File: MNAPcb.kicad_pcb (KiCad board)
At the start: 2 copper layers, 113.4 x 103.3 mm, 138 parts, among them J1 Conn_01x03_Pin, J2 DA15_Socket, J3 USB_C_Receptacle_USB2.0_16P, J5 Conn_01x02, J7 Conn_01x02, J8 Conn_01x04_Pin, J9 Conn_01x02, SW1 SW_Push_Shielded, U1 STM32F407VGTx, U10 USBLC6-2SC6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

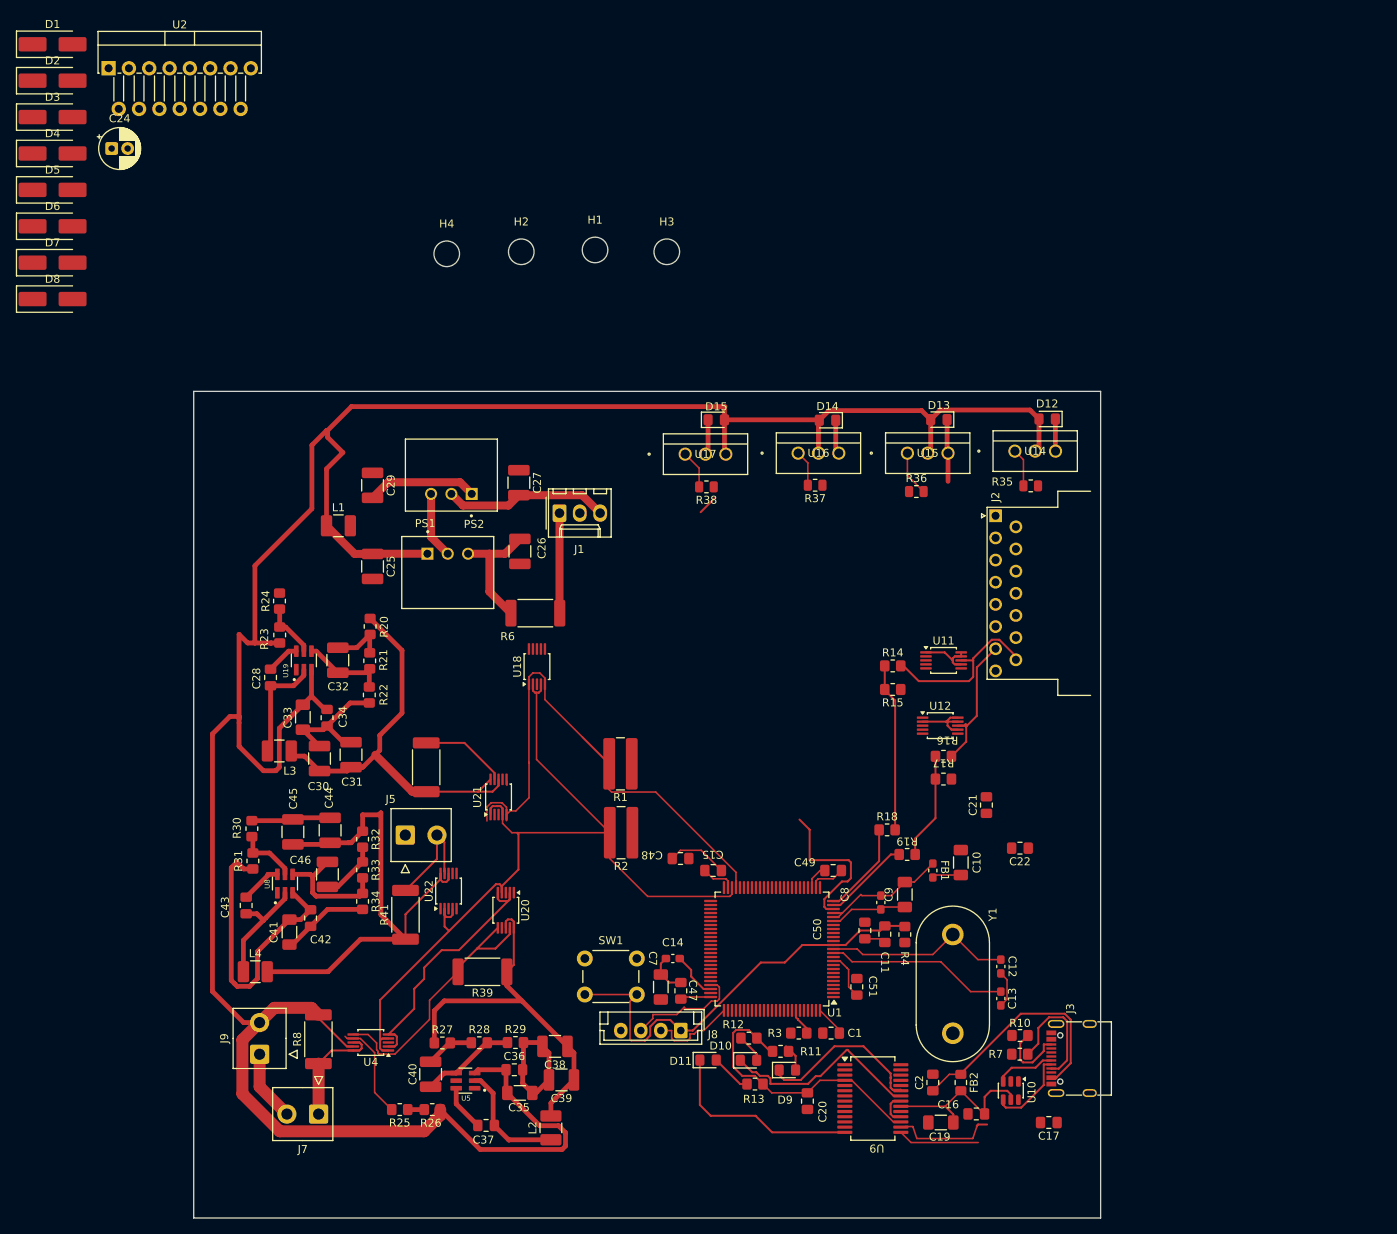
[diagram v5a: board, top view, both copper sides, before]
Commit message: Used Zones and Net
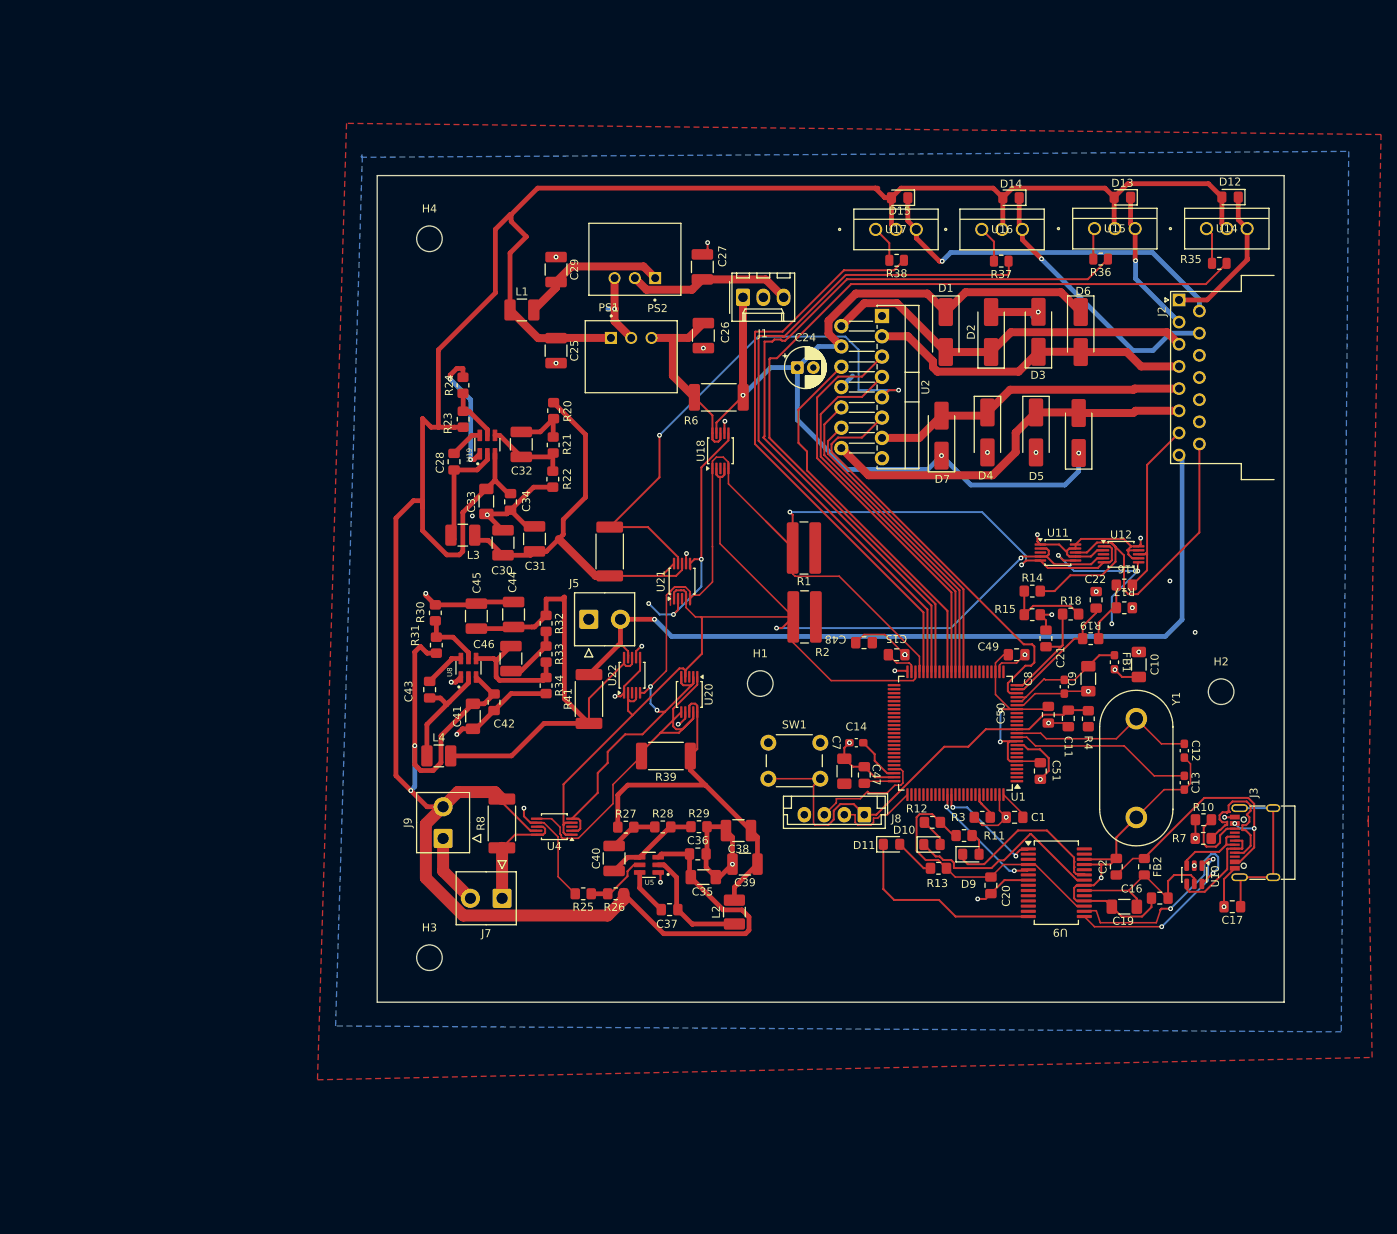
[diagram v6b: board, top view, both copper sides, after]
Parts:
- moved D8 129.4 mm to (170.1, 68.6), turned to 90 degrees
- moved D6 129.2 mm to (170.4, 56.0), turned to -90 degrees
- moved D5 126.6 mm to (164.8, 68.6), turned to -90 degrees
- moved D3 126.1 mm to (165.1, 56.0), turned to 90 degrees
- moved D4 122.0 mm to (158.7, 68.6), turned to -90 degrees
- moved D2 121.5 mm to (159.2, 56.0), turned to 90 degrees
- moved D1 117.3 mm to (153.5, 56.0), turned to -90 degrees
- moved D7 113.2 mm to (153.0, 69.0), turned to 90 degrees
- moved H2 103.3 mm to (187.9, 101.0)
- moved U2 101.5 mm to (145.5, 54.0), turned to -90 degrees
- moved H3 93.1 mm to (89.0, 134.2)
- moved C24 90.0 mm to (134.9, 60.5)
- moved H1 58.0 mm to (130.3, 99.9)
- moved R36 37.1 mm to (172.8, 46.9), turned to 180 degrees
- moved R38 37.0 mm to (147.3, 47.0)
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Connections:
- D13 pad 1: /ADC/POT2_V -> /RelayControl/K2OUT
- J2 pad 1: /L298/MOTOR1+ -> /RelayControl/K1OUT
- J2 pad 10: /L298/MOTOR2- -> /RelayControl/K3OUT
- J2 pad 11: GND -> unconnected-(J2-P111-Pad11)
- J2 pad 13: /RelayControl/K4OUT -> unconnected-(J2-P13-Pad13)
- J2 pad 14: /RelayControl/K3OUT -> GND
- J2 pad 2: /L298/MOTOR2+ -> /RelayControl/K2OUT
- J2 pad 3: GND -> /L298/MOTOR1+
- J2 pad 4: unconnected-(J2-Pad4) -> /L298/MOTOR1-
- J2 pad 5: unconnected-(J2-Pad5) -> /L298/MOTOR2+
- J2 pad 6: /RelayControl/K1OUT -> /L298/MOTOR2-
- J2 pad 9: /L298/MOTOR1- -> /RelayControl/K4OUT
- U1 pad 36: unconnected-(U1-PB1-Pad36) -> /L298/IN4
- U1 pad 37: unconnected-(U1-PB2-Pad37) -> /L298/IN3
- U1 pad 38: /L298/IN4 -> /L298/IN2
- U1 pad 39: /L298/IN3 -> /L298/IN1
- U1 pad 41: /L298/IN2 -> unconnected-(U1-PE10-Pad41)
- U1 pad 42: /L298/IN1 -> unconnected-(U1-PE11-Pad42)
- U15 pad 3: /ADC/POT2_V -> /RelayControl/K2OUT
- U17 pad 2: /RelayControl/K4OUT -> +24
- U17 pad 3: +24 -> /RelayControl/K4OUT
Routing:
- net GND: track 143.4 -> 271.1 mm, vias 0 -> 43
- net +15: track 12.5 -> 122.6 mm, vias 0 -> 3
- net /MCU/K1IN: track 0.00 -> 109.8 mm
- net +3.3: track 49.3 -> 148.4 mm, vias 0 -> 11
- net /MCU/K2IN: track 0.00 -> 97.4 mm
- net +12: track 13.9 -> 104.0 mm, vias 0 -> 1
- net /MCU/K3IN: track 0.00 -> 87.0 mm
- net /ADC/SCL_ADC: track 104.3 -> 178.1 mm, vias 0 -> 4
- net /MCU/K4IN: track 0.00 -> 73.5 mm
- net +5: track 10.9 -> 68.1 mm, vias 0 -> 2
- net /L298/IN1: track 0.00 -> 51.5 mm
- net /ADC/SDA_ADC: track 108.5 -> 158.4 mm, vias 0 -> 2
- net /L298/IN2: track 0.00 -> 48.8 mm
- net /L298/MOTOR2-: track 0.00 -> 48.5 mm
- net /L298/PWM1: track 0.00 -> 48.1 mm
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- added copper zone on F.Cu, net +3.3
- added copper zone on B.Cu, net GND

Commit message: Solved all the Erros
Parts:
- J3: footprint Connector_USB:USB_C_Receptacle_G-Switch_GT-USB-7010ASV -> Connector_USB:USB_C_Receptacle_Palconn_UTC16-G
- moved R12 19.6 mm to (169.5, 125.8)
- moved U10 19.2 mm to (166.4, 130.0), turned to 90 degrees
- moved D10 15.1 mm to (165.7, 125.8)
- moved R11 14.2 mm to (169.7, 122.0), turned to 0 degrees
- moved R7 13.5 mm to (183.2, 132.6), turned to -90 degrees
- moved D11 10.5 mm to (151.5, 129.3), turned to 180 degrees
- moved FB2 9.27 mm to (171.3, 128.9), turned to 180 degrees
- moved D9 9.08 mm to (165.7, 122.0)
- moved C2 8.83 mm to (183.6, 121.9)
- moved U9 8.82 mm to (158.5, 125.1)
- moved C20 8.23 mm to (161.7, 133.0), turned to 0 degrees
- moved R13 8.22 mm to (147.3, 129.3), turned to 180 degrees
- moved J3 7.70 mm to (190.9, 127.1)
- moved C19 7.48 mm to (171.2, 133.8)
- moved C17 6.98 mm to (186.7, 134.3)
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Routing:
- net GND: track 271.1 -> 319.6 mm, vias 43 -> 35
- net +3.3: track 148.4 -> 177.8 mm, vias 11 -> 15
- net Net-(D10-K): track 25.8 -> 3.13 mm
- net Net-(D11-K): track 25.1 -> 2.49 mm
- net Net-(U9-USBD+): track 23.1 -> 4.20 mm, vias 2 -> 0
- net Net-(D9-K): track 21.3 -> 3.95 mm
- net /UART/D+: track 9.47 -> 26.1 mm, vias 0 -> 2
- net /UART/D-: track 13.4 -> 29.2 mm, vias 0 -> 3
- net Net-(J3-CC1): track 19.4 -> 6.52 mm
- net Net-(U9-USBD-): track 15.7 -> 3.53 mm, vias 2 -> 0
- net /UART/VCCIO: track 35.3 -> 45.3 mm, vias 0 -> 3
- net /ADC/SCL_ADC: track 178.1 -> 170.9 mm
- net /MCU/USART_RX: track 14.1 -> 7.37 mm, vias 2 -> 0
- net /ADC/SDA_ADC: track 158.4 -> 161.5 mm
- net Net-(D11-A): track 5.08 -> 2.17 mm
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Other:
- board text added: "GND"
- board text added: "NRST"
- board text added: "SWCLK"
- board text added: "SWDIO"
